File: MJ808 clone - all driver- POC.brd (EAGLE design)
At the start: 35.5 x 35.5 mm, 39 parts, among them IC1 ATTINY4313-MMH, IC2 PRQV8.00CR1510Y00L, IC6 MCP2515, IC7 MAX16820, IC8 MCP2561-2, IC9 TPS709-Q1, K1 CRTL, Q1 PMV213SN,215, X1 22-23-2021, X2 22-23-2021

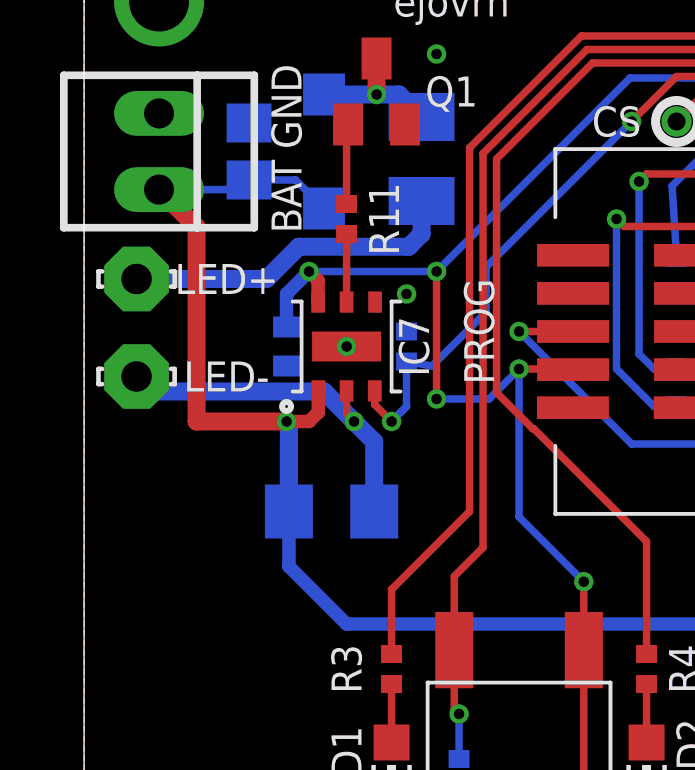
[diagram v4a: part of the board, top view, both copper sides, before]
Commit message: - replaced LED connector with 2.54mm pitch header
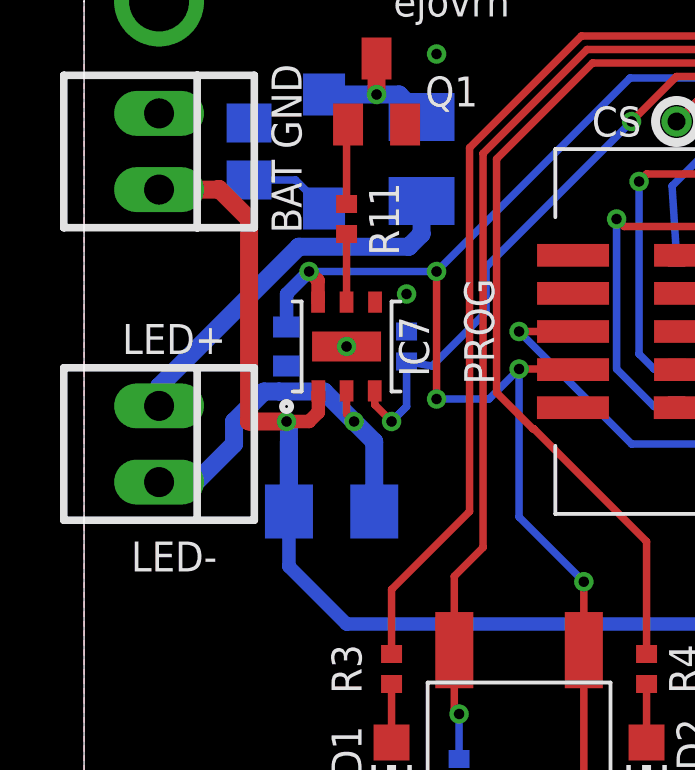
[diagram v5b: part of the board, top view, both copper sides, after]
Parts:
- removed LSP1, LSP2: LSP10, solpad:LSP10
- added X3: 22-23-2021, con-molex:22-23-2021
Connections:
- removed net N$3: L1.2, LSP2.MP
- new net LED+: L1.2, X3.1
- net CSN: now also X3.2; no longer LSP1.MP
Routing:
- net LED+: track 0.00 -> 12.6 mm
- net N$3: track 11.2 -> 0.00 mm
- net CSN: track 12.3 -> 13.0 mm
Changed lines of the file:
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@@
 <?xml version="1.0" encoding="utf-8"?>
 <!DOCTYPE eagle SYSTEM "eagle.dtd">
-<eagle version="8.6.1">
+<eagle version="8.6.3">
 <drawing>
 <settings>
@@
 <text x="12.25" y="34.5" size="1" layer="21" font="vector" align="center">MJ-808 clone POC</text>
 <text x="12.25" y="33" size="1" layer="21" font="vector" align="center">ejovrh</text>
-<text x="4.75" y="23.75" size="1" layer="21" font="vector" align="center">LED+</text>
-<text x="4.75" y="20.5" size="1" layer="21" font="vector" rot="R180" align="center">LED-</text>
+<text x="3" y="21.75" size="1" layer="21" font="vector" align="center">LED+</text>
+<text x="3" y="14.5" size="1" layer="21" font="vector" align="center">LED-</text>
 <wire x1="2.5" y1="0" x2="33" y2="0" width="0" layer="20"/>
 <wire x1="35.5" y1="2.5" x2="35.5" y2="33" width="0" layer="20"/>
@@
 <attribute name="SPICEPREFIX" value="L" x="11.25" y="27.75" size="1.778" layer="28" rot="MR270" display="off"/>
 </element>
-<element name="LSP1" library="solpad" library_urn="urn:adsk.eagle:library:364" package="LSP10" package3d_urn="urn:adsk.eagle:package:26501/1" value="LSP10" x="1.75" y="20.5" smashed="yes">
-<attribute name="VALUE" x="1.75" y="20.754" size="0.0254" layer="27"/>
-</element>
-<element name="LSP2" library="solpad" library_urn="urn:adsk.eagle:library:364" package="LSP10" package3d_urn="urn:adsk.eagle:package:26501/1" value="LSP10" x="1.75" y="23.75" smashed="yes">
-<attribute name="VALUE" x="1.75" y="24.004" size="0.0254" layer="27"/>
-</element>
 <element name="Q1" library="adafruit" library_urn="urn:adsk.eagle:library:420" package="SOT23" value="PMV213SN,215" x="9.75" y="30" smashed="yes">
 <attribute name="NAME" x="12.25" y="30" size="1" layer="25" font="vector" align="center"/>
@@
 <attribute name="SPICEPREFIX" value="R" x="33.17" y="13.5" size="1.778" layer="28" rot="MR90" display="off"/>
 <attribute name="VALUE" x="31.265" y="12.865" size="1.27" layer="28" rot="MR90"/>
+</element>
+<element name="X3" library="con-molex" library_urn="urn:adsk.eagle:library:165" package="22-23-2021" value="22-23-2021" x="2.5" y="18.25" smashed="yes" rot="R270">
+<attribute name="MF" value="MOLEX" x="2.5" y="18.25" size="1.778" layer="27" rot="R270" display="off"/>
+<attribute name="MPN" value="22-23-2021" x="2.5" y="18.25" size="1.778" layer="27" rot="R270" display="off"/>
+<attribute name="OC_FARNELL" value="1462926" x="2.5" y="18.25" size="1.778" layer="27" rot="R270" display="off"/>
+<attribute name="OC_NEWARK" value="25C3832" x="2.5" y="18.25" size="1.778" layer="27" rot="R270" display="off"/>
+<attribute name="VALUE" x="-2.58" y="20.79" size="1.016" layer="27" ratio="10" rot="R270"/>
 </element>
 </elements>
@@
 <wire x1="7.81" y1="19.31" x2="7.5" y2="19" width="0.45" layer="1"/>
 <wire x1="7.5" y1="19" x2="6.75" y2="19" width="0.45" layer="1"/>
-<wire x1="6.75" y1="19" x2="3.75" y2="19" width="0.6" layer="1"/>
+<wire x1="6.75" y1="19" x2="5.5" y2="19" width="0.6" layer="1"/>
 <wire x1="25.94" y1="5.56" x2="26" y2="5.5" width="0.45" layer="1"/>
 <wire x1="25.94" y1="9.56" x2="26" y2="9.5" width="0.45" layer="1"/>
 <wire x1="26" y1="5.5" x2="26" y2="9.5" width="0.45" layer="16"/>
 <wire x1="26" y1="12.25" x2="26" y2="9.5" width="0.45" layer="16"/>
-<wire x1="3.75" y1="25.48" x2="2.5" y2="26.73" width="0.6" layer="1"/>
-<wire x1="3.75" y1="19" x2="3.75" y2="25.48" width="0.6" layer="1"/>
 <contactref element="IC9" pad="IN"/>
 <wire x1="31.16924375" y1="12.25" x2="26" y2="12.25" width="0.25" layer="16"/>
@@
 <via x="6.75" y="19" extent="1-16" drill="0.35"/>
 <wire x1="6.828" y1="16" x2="6.828" y2="18.922" width="0.6" layer="16"/>
+<wire x1="5.5" y1="25.75" x2="4.5" y2="26.75" width="0.6" layer="1"/>
+<wire x1="4.5" y1="26.75" x2="4.48" y2="26.73" width="0.6" layer="1"/>
+<wire x1="4.48" y1="26.73" x2="2.5" y2="26.73" width="0.6" layer="1"/>
+<wire x1="5.5" y1="19" x2="5.5" y2="25.75" width="0.6" layer="1"/>
 </signal>
 <signal name="GND">
@@
 <via x="8.75" y="21.5" extent="1-16" drill="0.35"/>
 <contactref element="R5" pad="1"/>
-<wire x1="31.75" y1="28" x2="33" y2="33" width="0" layer="19" extent="1-1"/>
-<wire x1="29.25" y1="26.75" x2="31.75" y2="28" width="0" layer="19" extent="1-1"/>
-<wire x1="29.75" y1="25.26" x2="29.25" y2="26.75" width="0" layer="19" extent="1-1"/>
-<wire x1="29.75" y1="23.9" x2="29.75" y2="25.26" width="0" layer="19" extent="1-16"/>
-<wire x1="29.75" y1="23.26" x2="29.75" y2="23.9" width="0" layer="19" extent="1-16"/>
-<wire x1="27.5" y1="28.25" x2="29.25" y2="26.75" width="0" layer="19" extent="16-16"/>
-<wire x1="25.9" y1="30.4" x2="27.5" y2="28.25" width="0" layer="19" extent="16-16"/>
-<wire x1="24.75" y1="30.5" x2="24.25" y2="30.4" width="0" layer="19" extent="1-16"/>
-<wire x1="24.75" y1="31.85" x2="24.75" y2="30.5" width="0" layer="19" extent="1-1"/>
-<wire x1="24.75" y1="33.25" x2="24.75" y2="31.85" width="0" layer="19" extent="1-1"/>
-<wire x1="33.15" y1="18.8" x2="29.75" y2="23.26" width="0" layer="19" extent="1-16"/>
-<wire x1="32.5" y1="17.75" x2="33.15" y2="18.8" width="0" layer="19" extent="16-16"/>
-<wire x1="31.75" y1="15.5" x2="32.5" y2="17.75" width="0" layer="19" extent="16-16"/>
-<wire x1="30.075" y1="15.825" x2="31.75" y2="15.5" width="0" layer="19" extent="1-1"/>
-<wire x1="28.75" y1="14.85" x2="29.75" y2="15.5" width="0" layer="19" extent="1-16"/>
-<wire x1="27.75" y1="15.5" x2="28.75" y2="14.85" width="0" layer="19" extent="16-16"/>
-<wire x1="33.5" y1="10" x2="31.75" y2="15.5" width="0" layer="19" extent="1-1"/>
-<wire x1="33" y1="2.5" x2="33.5" y2="10" width="0" layer="19" extent="1-1"/>
-<wire x1="16.3" y1="24.54" x2="24.25" y2="30.4" width="0" layer="19" extent="1-16"/>
-<wire x1="16.295" y1="19.46" x2="16.3" y2="24.54" width="0" layer="19" extent="1-1"/>
-<wire x1="10.75" y1="23.25" x2="16.3" y2="24.54" width="0" layer="19" extent="1-1"/>
-<wire x1="9.7" y1="22.98" x2="10.75" y2="23.25" width="0" layer="19" extent="1-1"/>
-<wire x1="10.75" y1="22" x2="10.75" y2="23.25" width="0" layer="19" extent="16-16"/>
-<wire x1="8.75" y1="21.5" x2="9.7" y2="22.98" width="0" layer="19" extent="1-1"/>
-<wire x1="6.75" y1="20.85" x2="8.75" y2="21.5" width="0" layer="19" extent="1-16"/>
-<wire x1="10.7" y1="28.9" x2="10.75" y2="23.25" width="0" layer="19" extent="1-1"/>
-<wire x1="11.75" y1="31.25" x2="10.7" y2="28.9" width="0" layer="19" extent="1-1"/>
-<wire x1="5.5" y1="28.95" x2="10.7" y2="28.9" width="0" layer="19" extent="1-16"/>
-<wire x1="2.5" y1="29.27" x2="5.5" y2="28.95" width="0" layer="19" extent="16-16"/>
-<wire x1="2.5" y1="33" x2="2.5" y2="29.27" width="0" layer="19" extent="1-1"/>
-<wire x1="12.5" y1="6.75" x2="16.295" y2="19.46" width="0" layer="19" extent="1-16"/>
-<wire x1="2.5" y1="2.5" x2="12.5" y2="6.75" width="0" layer="19" extent="16-16"/>
-<wire x1="33.17" y1="13" x2="2.5" y2="2.5" width="0" layer="19" extent="1-1"/>
+<wire x1="29.75" y1="23.9" x2="29.75" y2="23.26" width="0" layer="19" extent="1-16"/>
+<wire x1="29.75" y1="15.5" x2="28.75" y2="14.85" width="0" layer="19" extent="1-16"/>
 </signal>
 <signal name="DIM_FRONT">
@@
 </signal>
 <signal name="CSN">
-<contactref element="LSP1" pad="MP"/>
 <contactref element="IC7" pad="CSN"/>
 <contactref element="R10" pad="1"/>
@@
 <via x="9" y="19" extent="1-16" drill="0.35"/>
 <wire x1="8" y1="20" x2="9" y2="19" width="0.6" layer="16"/>
-<wire x1="1.75" y1="20.5" x2="2.25" y2="20" width="0.6" layer="16"/>
-<wire x1="2.25" y1="20" x2="8" y2="20" width="0.6" layer="16"/>
+<wire x1="6" y1="20" x2="6.5" y2="20" width="0.6" layer="16"/>
+<wire x1="8" y1="20" x2="6.5" y2="20" width="0.6" layer="16"/>
 <wire x1="9" y1="19" x2="9.672" y2="18.328" width="0.6" layer="16"/>
 <wire x1="9.672" y1="18.328" x2="9.672" y2="16" width="0.6" layer="16"/>
+<contactref element="X3" pad="2"/>
+<wire x1="2.5" y1="16.98" x2="3.73" y2="16.98" width="0.6" layer="16"/>
+<wire x1="3.73" y1="16.98" x2="5" y2="18.25" width="0.6" layer="16"/>
+<wire x1="5" y1="18.25" x2="5" y2="19" width="0.6" layer="16"/>
+<wire x1="5" y1="19" x2="6" y2="20" width="0.6" layer="16"/>
+<wire x1="6.5" y1="20" x2="6.5" y2="20" width="0.6" layer="16"/>
 </signal>
 <signal name="SPI_MISO">
@@
 <wire x1="8.75" y1="22.98" x2="8.75" y2="25.25" width="0.25" layer="1"/>
 </signal>
-<signal name="N$3">
+<signal name="LED+">
 <contactref element="L1" pad="2"/>
-<contactref element="LSP2" pad="MP"/>
-<wire x1="1.75" y1="23.75" x2="6.08326875" y2="23.75" width="0.6" layer="16"/>
-<wire x1="6.08326875" y1="23.75" x2="7.15826875" y2="24.825" width="0.6" layer="16"/>
-<wire x1="10.825" y1="24.825" x2="7.15826875" y2="24.825" width="0.6" layer="16"/>
+<wire x1="7.15826875" y1="24.825" x2="10.825" y2="24.825" width="0.6" layer="16"/>
 <wire x1="11.25" y1="26.35" x2="11.25" y2="25.25" width="0.6" layer="16"/>
-<wire x1="11.25" y1="25.25" x2="10.825" y2="24.825" width="0.6" layer="16"/>
+<wire x1="10.825" y1="24.825" x2="11.25" y2="25.25" width="0.6" layer="16"/>
+<contactref element="X3" pad="1"/>
+<wire x1="2.5" y1="19.52" x2="2.5" y2="20.16673125" width="0.6" layer="16"/>
+<wire x1="2.5" y1="20.16673125" x2="7.15826875" y2="24.825" width="0.6" layer="16"/>
 </signal>
 <signal name="DEBUGWIRE/RESET">
@@
 <wire x1="33.165378125" y1="28.334621875" x2="29" y2="32.5" width="0.25" layer="1"/>
 <contactref element="R5" pad="2"/>
-<wire x1="33.165378125" y1="15.584621875" x2="33.17" y2="14" width="0" layer="19" extent="1-16"/>
+<wire x1="33.17" y1="14" x2="33.165378125" y2="15.584621875" width="0" layer="19" extent="16-16"/>
 </signal>
 <signal name="SWITCH">

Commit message: - corrected DRC issues
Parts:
- moved C5 2.33 mm to (31.1, 21.4), turned to 180 degrees
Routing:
- net GND: track 3.48 -> 8.62 mm, vias 13 -> 15
- net EN: track 23.6 -> 25.2 mm
- net 5V0_REG: track 16.2 -> 17.4 mm
- net DIM_FRONT: track 21.7 -> 20.9 mm

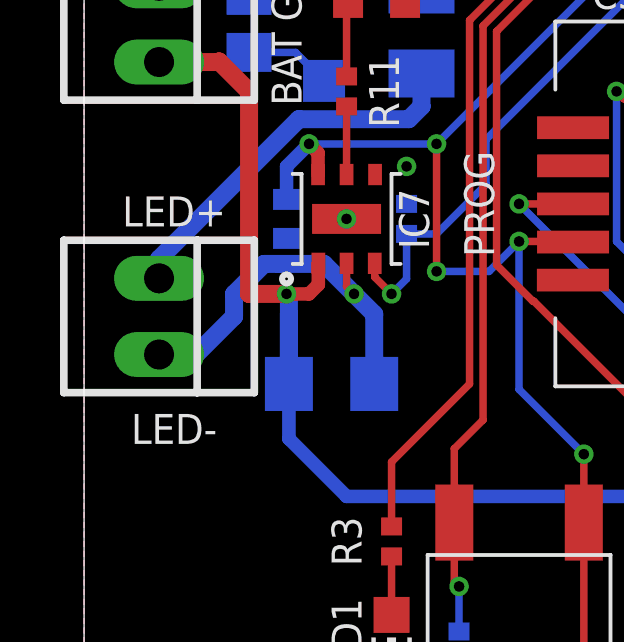
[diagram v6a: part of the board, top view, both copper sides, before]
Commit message: - corrected LED plus and minus signs on connector
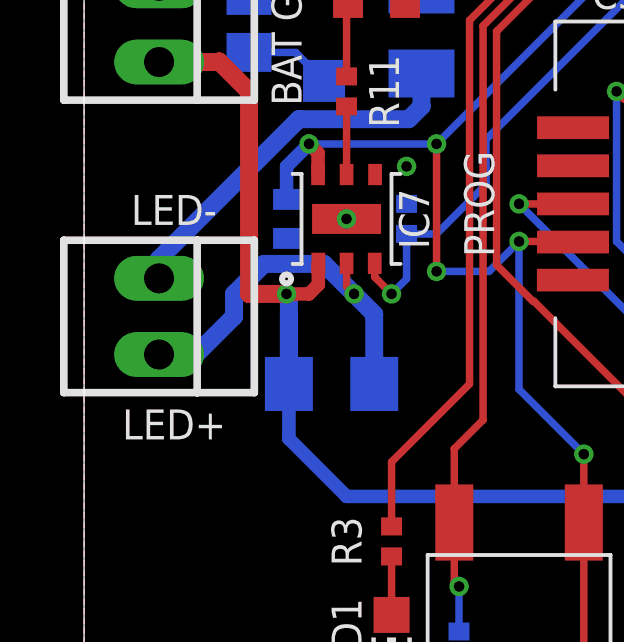
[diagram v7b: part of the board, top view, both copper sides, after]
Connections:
- net LED1 renamed RED_LED
- net LED2 renamed GREEN_LED
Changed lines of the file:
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@@
 <text x="12.25" y="34.5" size="1" layer="21" font="vector" align="center">MJ-808 clone POC</text>
 <text x="12.25" y="33" size="1" layer="21" font="vector" align="center">ejovrh</text>
-<text x="3" y="21.75" size="1" layer="21" font="vector" align="center">LED+</text>
-<text x="3" y="14.5" size="1" layer="21" font="vector" align="center">LED-</text>
+<text x="3" y="14.65" size="1" layer="21" font="vector" align="center">LED+</text>
+<text x="3" y="21.8" size="1" layer="21" font="vector" align="center">LED-</text>
 <wire x1="2.5" y1="0" x2="33" y2="0" width="0" layer="20"/>
 <wire x1="35.5" y1="2.5" x2="35.5" y2="33" width="0" layer="20"/>
@@
 <wire x1="18.75" y1="8.3" x2="18.75" y2="10.25" width="0.25" layer="1"/>
 </signal>
-<signal name="LED1">
+<signal name="RED_LED">
 <contactref element="R3" pad="1"/>
 <contactref element="IC1" pad="PB0"/>
@@
 <wire x1="10.25" y1="13.4" x2="12.85" y2="16" width="0.25" layer="1"/>
 </signal>
-<signal name="LED2">
+<signal name="GREEN_LED">
 <contactref element="R4" pad="1"/>
 <contactref element="IC1" pad="PB2"/>
